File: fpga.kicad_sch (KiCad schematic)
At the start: 48 parts, among them Q1 BSS138PW, SW1 SW_B3U-1000P_SMD, U1 ICE40UP5K-SG48, U3 W25Q32JW_SOIC-8, Y1 Oscillator_12MHz_ESC_2520MV

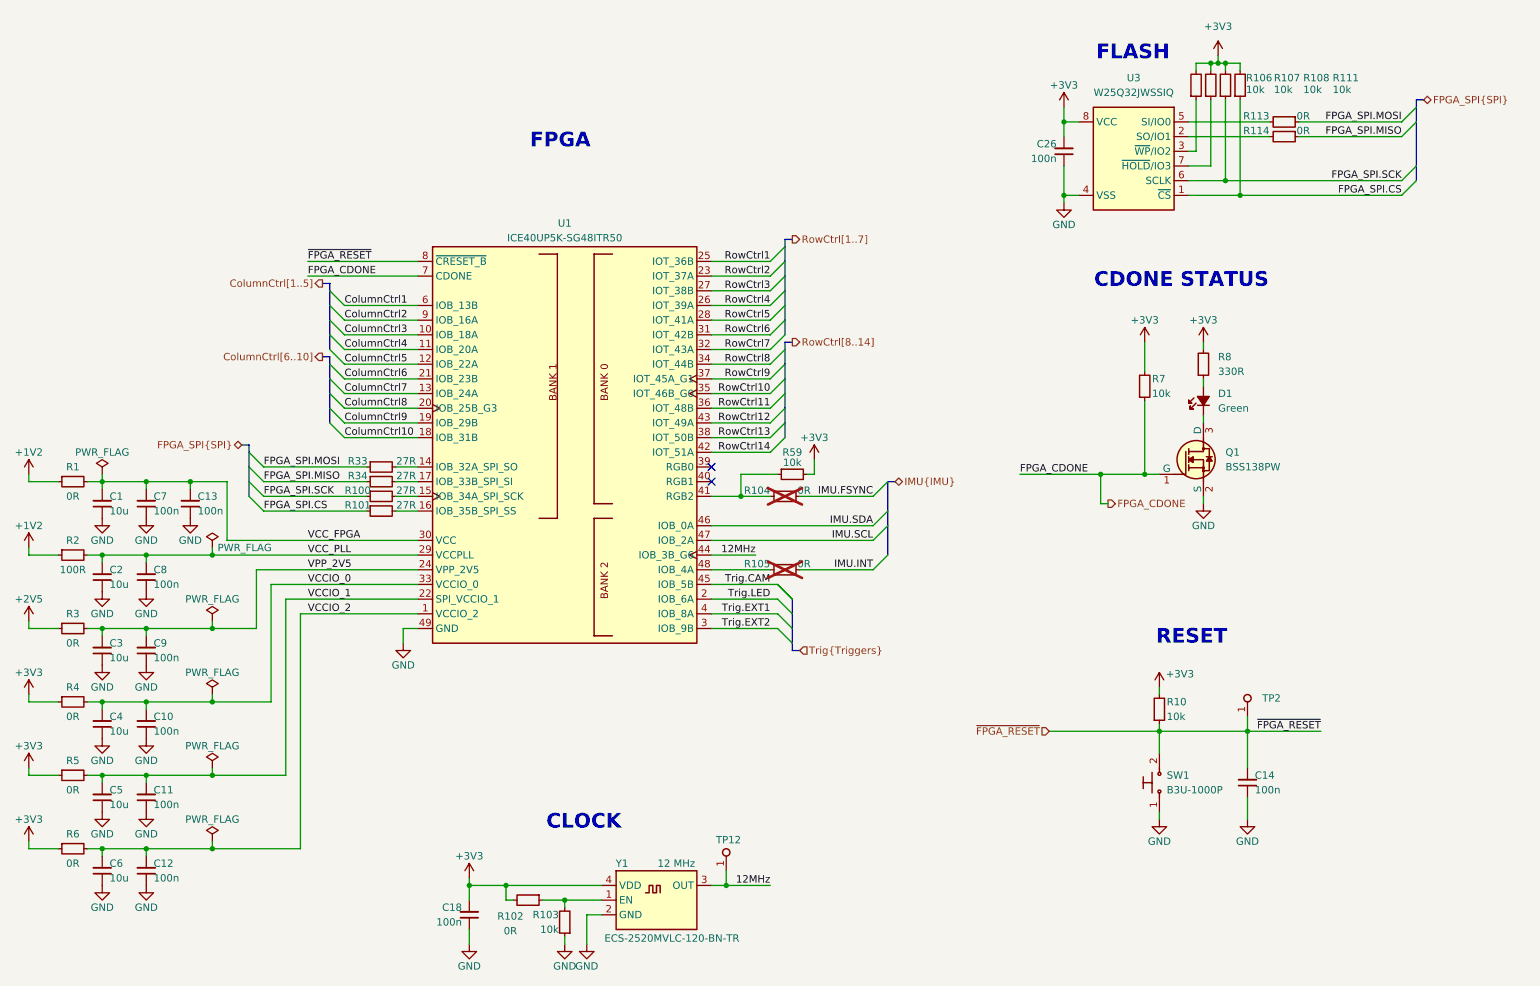
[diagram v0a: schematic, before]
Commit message: [#72447] Update designators
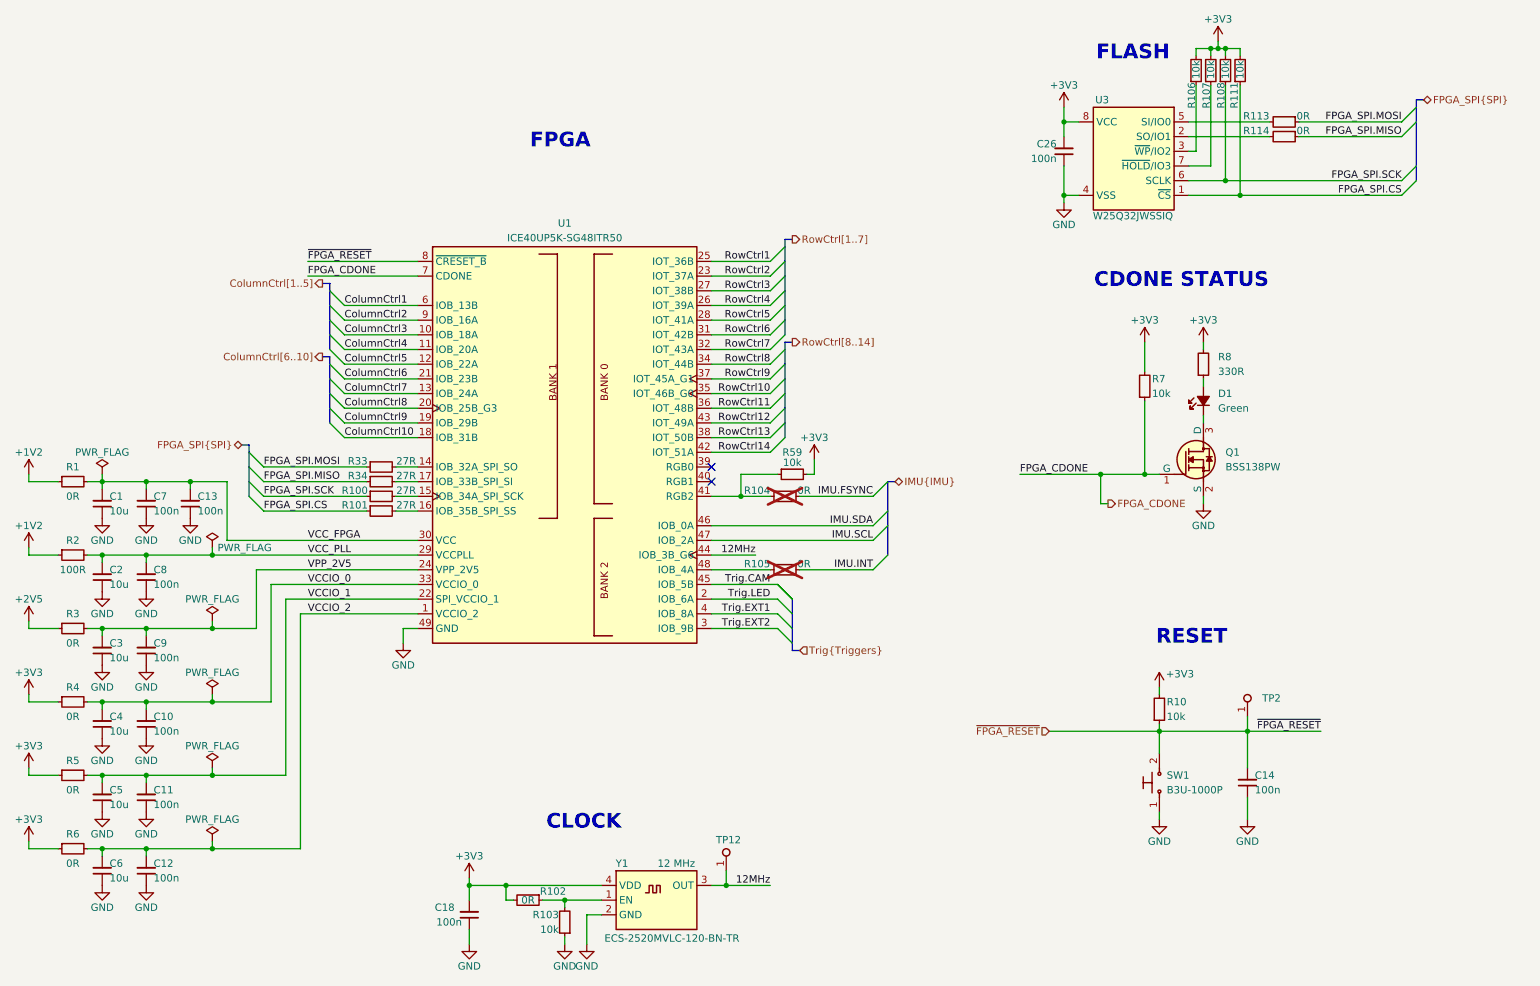
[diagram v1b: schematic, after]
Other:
- moved on the sheet: R106, R107, R108, R111
